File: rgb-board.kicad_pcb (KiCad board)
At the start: 2 copper layers, 178 x 129.5 mm, 89 parts, among them J1 Conn_02x25_Odd_Even, J10 Conn_Coaxial, J11 Conn_Coaxial, J2 SCART-F, J3 TEST_1P, J4 TEST_1P, J5 Conn_Coaxial, J6 Conn_Coaxial, J7 Conn_Coaxial, J8 Conn_Coaxial, J9 Conn_Coaxial, Q101 BC850C, Q105 BC850C, Q109 BC850C, Q113 BC850C, Q114 BC850C, Q201 BC850C, SW1 SW_DPDT_x2, U1 NCP1117-12_SOT223

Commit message: Add files via upload
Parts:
- removed C105: 10uF/50V, Capacitor_SMD:C_Elec_5x5.4
- removed C119: 100nF, Capacitor_SMD:C_0805_2012Metric_Pad1.18x1.45mm_HandSolder
- removed D109, D110: BAT46-TR, Diode_SMD:D_SOD-123
- removed J5, J6, J7, J8, J9: Conn_Coaxial, bnc-tht:BNC-THT
- removed Q114: BC850C, Package_TO_SOT_SMD:SOT-23_Handsoldering
- removed R152: 75, Resistor_SMD:R_0805_2012Metric_Pad1.20x1.40mm_HandSolder
- removed R155: 100, Resistor_SMD:R_0805_2012Metric_Pad1.20x1.40mm_HandSolder
- removed R156, R157: 33k, Resistor_SMD:R_0805_2012Metric_Pad1.20x1.40mm_HandSolder
- removed R158: 2.7k, Resistor_SMD:R_0805_2012Metric_Pad1.20x1.40mm_HandSolder
- added C1: 1uF/16V, Capacitor_SMD:C_Elec_4x5.4, F.Cu at (115.7, 43.4)
- added C2: 1uF/16V, Capacitor_SMD:C_Elec_4x5.4, F.Cu at (115.7, 57.1)
- added C3: 100nF, Capacitor_SMD:C_1206_3216Metric_Pad1.33x1.80mm_HandSolder, F.Cu at (124.8, 56.5)
- added C4: 10nF, Capacitor_SMD:C_1206_3216Metric_Pad1.33x1.80mm_HandSolder, F.Cu at (153.3, 51.6)
- added C5: 10nF, Capacitor_SMD:C_1206_3216Metric_Pad1.33x1.80mm_HandSolder, F.Cu at (137.6, 55.4)
- added C6: 100nF, Capacitor_SMD:C_1206_3216Metric_Pad1.33x1.80mm_HandSolder, F.Cu at (146.5, 56.4)
- added D1: 1N4148W, Diode_SMD:D_SOD-123, F.Cu at (137.6, 47.9)
- added D2: LED_Small_Filled, LED_THT:LED_D5.0mm_Horizontal_O1.27mm_Z3.0mm, F.Cu at (88.5, 66.2)
- added J4: TEST_1P, Mounting_Holes:MountingHole_3.2mm_M3, F.Cu at (97.0, 152.2)
- added J4: TEST_1P, Mounting_Holes:MountingHole_3.2mm_M3, F.Cu at (102.5, 38.2)
- added Q1: BC847B, Package_TO_SOT_SMD:SOT-23_Handsoldering, F.Cu at (132.4, 58.7)
- added R10: 470R, Resistor_SMD:R_1206_3216Metric_Pad1.30x1.75mm_HandSolder, F.Cu at (115.7, 62.2)
- added R11: 1k, Resistor_SMD:R_1206_3216Metric_Pad1.30x1.75mm_HandSolder, F.Cu at (137.6, 51.5)
- added R4: 10k, Resistor_SMD:R_1206_3216Metric_Pad1.30x1.75mm_HandSolder, F.Cu at (115.6, 48.4)
- added R5: 10k, Resistor_SMD:R_1206_3216Metric_Pad1.30x1.75mm_HandSolder, F.Cu at (115.6, 52.1)
- added R6: 2k2, Resistor_SMD:R_1206_3216Metric_Pad1.30x1.75mm_HandSolder, F.Cu at (131.6, 47.0)
- added R7: 1k, Resistor_SMD:R_1206_3216Metric_Pad1.30x1.75mm_HandSolder, F.Cu at (124.7, 60.2)
- added R8: 5k6, Resistor_SMD:R_1206_3216Metric_Pad1.30x1.75mm_HandSolder, F.Cu at (153.3, 45.9)
- added R9: 8k2, Resistor_SMD:R_1206_3216Metric_Pad1.30x1.75mm_HandSolder, F.Cu at (137.7, 44.0)
- added U2: 74HC86, Package_SO:SOIC-14_3.9x8.7mm_P1.27mm, F.Cu at (124.9, 50.5)
- added U3: 74HC123, Package_SO:SOIC-16_3.9x9.9mm_P1.27mm, F.Cu at (146.3, 49.6)
- added X1: VGAF, HD15:HD15_B-HD15F, F.Cu at (92.4, 49.5)
- C114, C116, C117, C118, C121, C201, C202, C204, C205, C206: footprint Capacitor_SMD:C_0805_2012Metric_Pad1.18x1.45mm_HandSolder -> Capacitor_SMD:C_1206_3216Metric_Pad1.33x1.80mm_HandSolder
- C120, C122: footprint Capacitor_SMD:C_Elec_5x5.4 -> Capacitor_SMD:C_Elec_4x5.4
- D101, D102, D103, D104, D105, D106, D107, D108: value BAT46-TR -> BAT46W
- D201: value D_Zener -> BZT52C12
- J10, J11: value Conn_Coaxial -> RCJ-013; footprint rcj-41x:RCJ-04X -> RCJ-013:CUI_RCJ-013
- J3: value TEST_1P -> AudioJack2_Ground_123; footprint Mounting_Holes:MountingHole_3.2mm_M3 -> Connector_PinHeader_2.54mm:PinHeader_1x03_P2.54mm_Vertical
- R1, R105, R106, R107, R119, R120, R121, R133, R134, R135, R147, R148, R149, R2, R204, R3: footprint Resistor_SMD:R_0805_2012Metric_Pad1.20x1.40mm_HandSolder -> Resistor_SMD:R_1206_3216Metric_Pad1.30x1.75mm_HandSolder
- R101, R115, R129, R143: value 75 -> 75R; footprint Resistor_SMD:R_0805_2012Metric_Pad1.20x1.40mm_HandSolder -> Resistor_SMD:R_1206_3216Metric_Pad1.30x1.75mm_HandSolder
- R104, R114, R118, R128, R132, R142, R146: value 100 -> 100R; footprint Resistor_SMD:R_0805_2012Metric_Pad1.20x1.40mm_HandSolder -> Resistor_SMD:R_1206_3216Metric_Pad1.30x1.75mm_HandSolder
- R113, R127, R141: value 390 -> 390R; footprint Resistor_SMD:R_0805_2012Metric_Pad1.20x1.40mm_HandSolder -> Resistor_SMD:R_1206_3216Metric_Pad1.30x1.75mm_HandSolder
- R202: value 1K -> 1k; footprint Resistor_SMD:R_0805_2012Metric_Pad1.20x1.40mm_HandSolder -> Resistor_SMD:R_1206_3216Metric_Pad1.30x1.75mm_HandSolder
- R203: value 56K -> 56k; footprint Resistor_SMD:R_0805_2012Metric_Pad1.20x1.40mm_HandSolder -> Resistor_SMD:R_1206_3216Metric_Pad1.30x1.75mm_HandSolder
- R205: value 2.7K -> 2.7k; footprint Resistor_SMD:R_0805_2012Metric_Pad1.20x1.40mm_HandSolder -> Resistor_SMD:R_1206_3216Metric_Pad1.30x1.75mm_HandSolder
- moved J4 134.4 mm to (98.5, 95.2)
- moved J3 86.1 mm to (98.5, 120.2), turned to 90 degrees
- moved C115 69.8 mm to (154.7, 91.6), turned to 180 degrees
- moved R141 62.5 mm to (145.6, 126.6), turned to 0 degrees
- moved R113 62.5 mm to (145.6, 95.4), turned to 0 degrees
- moved R127 62.4 mm to (145.6, 110.9), turned to 0 degrees
- moved R106 61.7 mm to (134.6, 94.4)
- moved R133 61.7 mm to (140.2, 126.6)
- moved R120 61.7 mm to (134.6, 109.9)
- moved R134 61.7 mm to (134.6, 125.6)
- moved R119 61.7 mm to (140.1, 110.9)
- moved R105 61.7 mm to (140.1, 95.4)
- moved R142 61.5 mm to (145.6, 122.6)
- moved R128 61.4 mm to (145.6, 106.9)
- moved R114 61.3 mm to (145.6, 91.4)
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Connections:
- net /B/B-Y renamed /B/B-Y
- net /G/Y renamed /G/Y
- net /HD/CS renamed /HD/CS
- net /R/R-Y renamed /R/R-Y
- J1 pad 10: (no net) -> unconnected-(J1-Pad10)
- J1 pad 15: (no net) -> unconnected-(J1-Pad15)
- J1 pad 16: (no net) -> unconnected-(J1-Pad16)
- J1 pad 17: (no net) -> unconnected-(J1-Pad17)
- J1 pad 18: (no net) -> unconnected-(J1-Pad18)
- J1 pad 20: (no net) -> unconnected-(J1-Pad20)
- J1 pad 22: (no net) -> unconnected-(J1-Pad22)
- J1 pad 23: (no net) -> unconnected-(J1-Pad23)
- J1 pad 24: (no net) -> unconnected-(J1-Pad24)
- J1 pad 26: (no net) -> unconnected-(J1-Pad26)
- J1 pad 27: (no net) -> unconnected-(J1-Pad27)
- J1 pad 28: (no net) -> unconnected-(J1-Pad28)
- J1 pad 29: (no net) -> unconnected-(J1-Pad29)
- J1 pad 30: (no net) -> unconnected-(J1-Pad30)
- J1 pad 32: (no net) -> unconnected-(J1-Pad32)
- J1 pad 33: (no net) -> unconnected-(J1-Pad33)
- J1 pad 34: (no net) -> unconnected-(J1-Pad34)
- J1 pad 35: (no net) -> unconnected-(J1-Pad35)
- J1 pad 36: (no net) -> unconnected-(J1-Pad36)
- J1 pad 37: (no net) -> unconnected-(J1-Pad37)
- J1 pad 38: (no net) -> unconnected-(J1-Pad38)
- J1 pad 40: (no net) -> unconnected-(J1-Pad40)
- J1 pad 42: (no net) -> unconnected-(J1-Pad42)
- J1 pad 43: (no net) -> unconnected-(J1-Pad43)
- J1 pad 44: (no net) -> unconnected-(J1-Pad44)
- J1 pad 45: (no net) -> unconnected-(J1-Pad45)
- J1 pad 46: (no net) -> unconnected-(J1-Pad46)
- J1 pad 8: (no net) -> unconnected-(J1-Pad8)
- J1 pad 9: (no net) -> unconnected-(J1-Pad9)
- J10 pad 2: GND -> /AUDIO_EXT_R
- J11 pad 2: GND -> /AUDIO_EXT_L
- J2 pad 1: (no net) -> unconnected-(J2-Pad1)
- J2 pad 10: (no net) -> unconnected-(J2-Pad10)
- J2 pad 12: (no net) -> unconnected-(J2-Pad12)
- J2 pad 14: (no net) -> unconnected-(J2-Pad14)
- J2 pad 16: (no net) -> unconnected-(J2-Pad16)
- J2 pad 19: (no net) -> unconnected-(J2-Pad19)
- J2 pad 3: (no net) -> unconnected-(J2-Pad3)
- J2 pad 8: (no net) -> unconnected-(J2-Pad8)
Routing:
- net /VD_: track 141.6 -> 0.00 mm
- net +5V: track 0.00 -> 123.6 mm, vias 0 -> 3
- net Net-(R4-Pad2): track 0.00 -> 105.8 mm, vias 0 -> 3
- net Net-(D1-Pad1): track 0.00 -> 80.2 mm, vias 0 -> 2
- net /B/B-Y: track 28.7 -> 96.0 mm, vias 0 -> 1
- net Net-(R5-Pad2): track 0.00 -> 55.5 mm, vias 0 -> 1
- net /R/R-Y: track 46.4 -> 97.8 mm
- net /G/Y: track 40.4 -> 76.9 mm, vias 0 -> 1
- net /Y: track 120.9 -> 91.2 mm, vias 0 -> 1
- net Net-(D2-Pad1): track 0.00 -> 29.1 mm
- net Net-(U2-Pad3): track 0.00 -> 26.1 mm, vias 0 -> 2
- net /AUDIO_: track 113.6 -> 90.7 mm, vias 0 -> 1
- net Net-(Q1-Pad3): track 0.00 -> 22.2 mm, vias 0 -> 2
- net /VCC+14V: track 81.8 -> 59.6 mm, vias 0 -> 1
- net Net-(C5-Pad1): track 0.00 -> 21.5 mm, vias 0 -> 2
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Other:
- board size 178 x 129.5 mm -> 145 x 130 mm
- net class Default removed
- rule pad_to_mask_clearance: 0.2 -> 0
- board text added: "1080/1035"
- board text added: "AUDIO"
- board text added: "All resistors and MLCC caps are 1206 R1,2,10: 470 Ω R3: 20 kΩ R4,5: 10 kΩ R6: 2.2 kΩ R7,11,202: 1 kΩ R8: 5.6 kΩ R9: 8.2 kΩ R101,115,129,143: 75 Ω R104,114,118,128,132,142,146: 100 Ω R105,119,133,203: 56 kΩ R106,120,134,147,148: 33 kΩ R107,121,135: 1.5 kΩ R113,127,141: 390 Ω R149,205: 2.7 kΩ R204: 68 kΩ"
- board text added: "BGP(HD)"
- board text added: "Blue"
- board text added: "C1,2: 1µF/16V E-cap C3,6,114,116,117,118,206: 100 nF/25V MLCC C4,5: 10nF MLCC C101,102,103: 47µF/25V E-cap C104: 10µF/50V E-cap C115,207: 100 µF/16V E-Cap C120,122: 10µF/25V E-cap C121: 1 µF/25V MLCC C201,202,205: 180 pF MLCC C203: 1 µF/50V E-Cap C204: 39 pF MLCC"
- board text added: "C_IN(VIDEO)"
- board text added: "D101-D108: BAT46W (SOD-123) D201: BZT52C12 (12V Zener, SOD-123) D1: 1N4148W (SOD-123) D2: 5 mm LED Q1,101,105,109,113,201: BC847B (SOT-23)"
- board text added: "FSC CL/BW"
- board text added: "Green"
- board text added: "H-Sync"
- board text added: "HD VD"
- board text added: "H_BLK"
- board text added: "INPUT_A/B"
- board text added: "In Audio L In Audio R GND"
- board text added: "JVC IF-C01COMG (RGB/YPbPr) SCART/VGA 15kHz SMD CLONE BOARD (2021) Martin Hejnfelt (martin@hejnfelt.com) (2024) makotoworkshop.org"
- board text added: "NTSC/PAL"
- board text added: "ON - EXTERNAL STEREO OFF - INTERNAL MONO"
- board text added: "Red"
- board text added: "SDA SCL"
- board text added: "SLOT_SCA1 SLOT_SCA2 SLOT_SCA3 SLOT_SCA4 SLOT_DET"
- board text added: "To protect the CRT If VGA signal is not 15kHz HD/CS and LED are OFF"
- board text added: "V-Sync"
- board text added: "VCC+14V VCC+14V"
- board text added: "VCC+7V VCC+7V"
- board text added: "Vin Sync"
- board text added: "X1: VGAF (SUB-D 15 HD) J1: Pin Header Angled 2x25 J2: SCART Ninigi right angled J3: Pin Header 1x3 J10,11: RCA AV RCJ-013 CUDevices SW1: LC2259EENP U1: NCP1117-12 (SOT-223) U2: 74HC86 (SOP-14) U3: 74HC123 (SOP-16)"
- board text added: "Y B-Y R-Y"
- board text added: "YC_DET"
- board text added: "in Audio L"
- board text added: "in Audio R"
- board text removed: "Bridge here for input (BNC) and don't mount SW1"
- board text removed: "D101-D110: BAT46W (SOD-123) D201: BZT52C12 (12V Zener, SOD-123) All transistors (Q101, Q102, ...): BC850 C101,102,103: 47uF/25V E-cap C104,105,120,122: 10uF/25V E-cap C115,207: 100 uF/16V E-Cap C114,116,117,118,119,206: 100 nF/25V MLCC C203: 1 uF/50V E-Cap C121: 1 uF/25V MLCC C201,202,205: 180 pF MLCC C204: 39 pF MLCC MLCC caps are 0805 R101,115,129,143,152: 75 Ohm R104,114,118,128,132,142,146,15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"
- board text removed: "Do NOT mount this section when using SCART"
- board text removed: "JVC IF-C01COMG (RGB/YPbPr) SCART/BNC SMD CLONE BOARD (2021) Martin Hejnfelt (martin@hejnfelt.com) Dual input idea credit goes to James Vanderloeff!"
- board text removed: "SW1 IN - EXTERNAL STEREO OUT - INTERNAL MONO"
- board text removed: "VD"

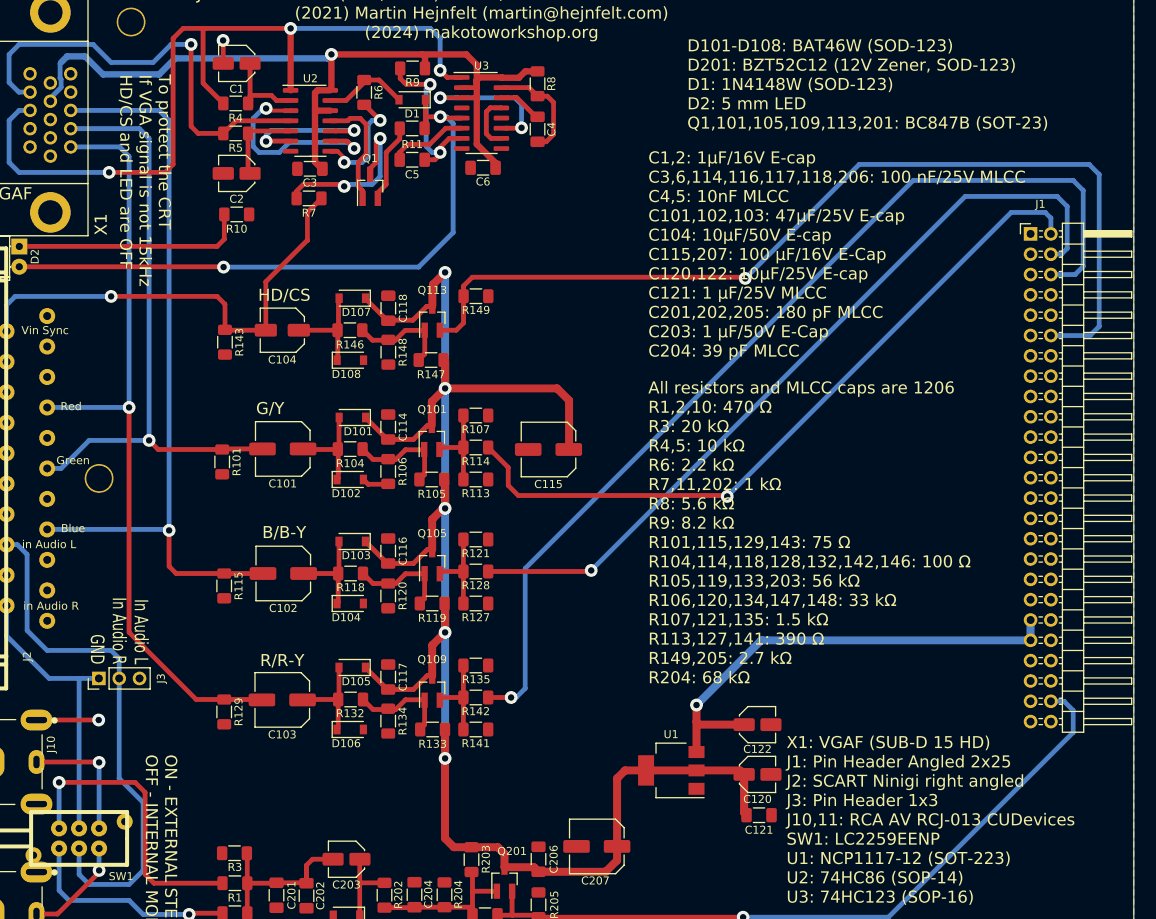
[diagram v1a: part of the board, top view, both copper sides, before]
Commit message: Update rgb-board.kicad_pcb
5V-corrigé
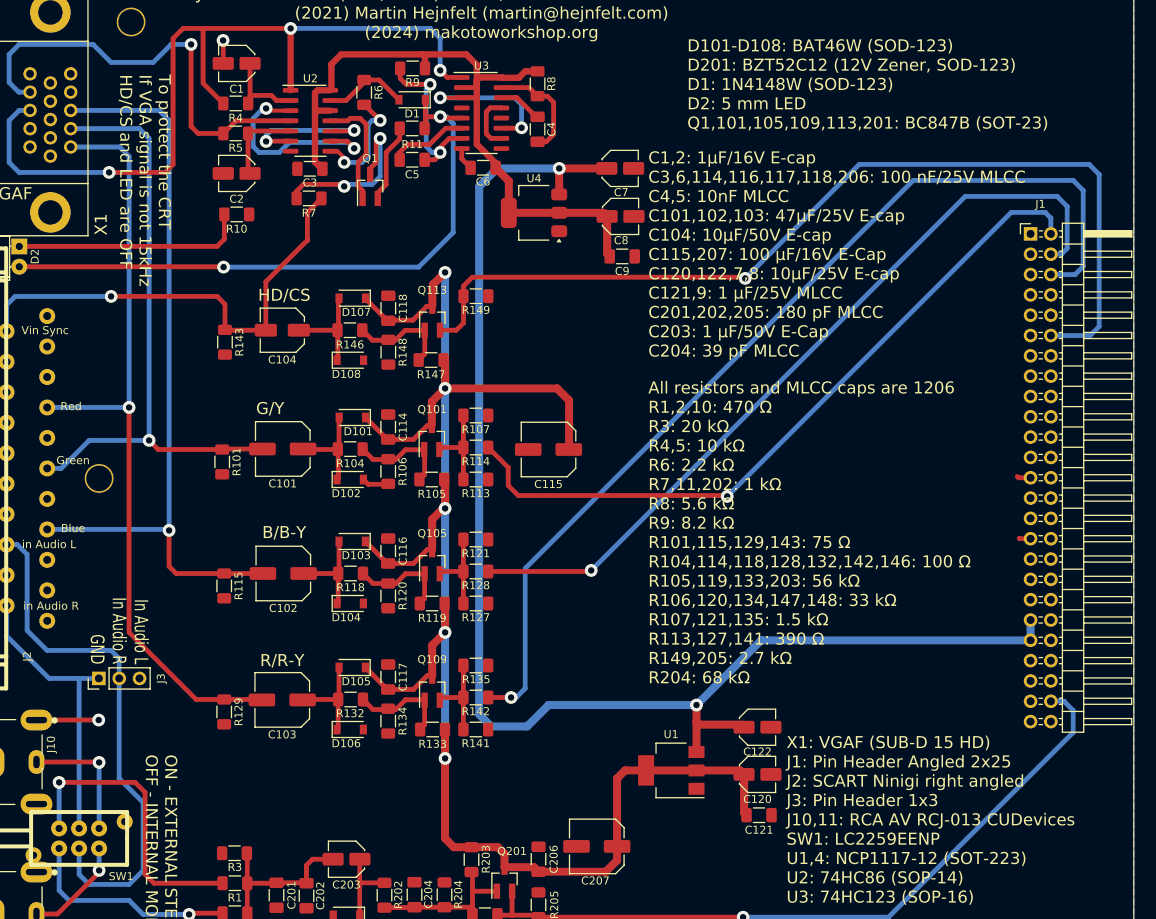
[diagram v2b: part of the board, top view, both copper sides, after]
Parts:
- added C7: 10uF/25V, Capacitor_SMD:C_Elec_4x5.4, F.Cu at (163.6, 56.5)
- added C8: 10uF/25V, Capacitor_SMD:C_Elec_4x5.4, F.Cu at (163.7, 62.5)
- added C9: 1uF/25V, Capacitor_SMD:C_1206_3216Metric_Pad1.33x1.80mm_HandSolder, F.Cu at (163.9, 67.5)
- added U4: NCP1117-5_SOT223, Package_TO_SOT_SMD:SOT-223-3_TabPin2, F.Cu at (152.8, 62.0)
- moved C122 0.33 mm to (180.8, 126.4)
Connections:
- X1 pad 9: +5V -> unconnected-(X1-Pad9)
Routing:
- net /VCC+14V: track 59.6 -> 174.7 mm, vias 1 -> 2
- net +5V: track 123.6 -> 105.9 mm, vias 3 -> 2
- net GND: track 14.1 -> 20.1 mm
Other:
- board text added: "C1,2: 1µF/16V E-cap C3,6,114,116,117,118,206: 100 nF/25V MLCC C4,5: 10nF MLCC C101,102,103: 47µF/25V E-cap C104: 10µF/50V E-cap C115,207: 100 µF/16V E-Cap C120,122,7,8: 10µF/25V E-cap C121,9: 1 µF/25V MLCC C201,202,205: 180 pF MLCC C203: 1 µF/50V E-Cap C204: 39 pF MLCC"
- board text added: "X1: VGAF (SUB-D 15 HD) J1: Pin Header Angled 2x25 J2: SCART Ninigi right angled J3: Pin Header 1x3 J10,11: RCA AV RCJ-013 CUDevices SW1: LC2259EENP U1,4: NCP1117-12 (SOT-223) U2: 74HC86 (SOP-14) U3: 74HC123 (SOP-16)"
- board text removed: "C1,2: 1µF/16V E-cap C3,6,114,116,117,118,206: 100 nF/25V MLCC C4,5: 10nF MLCC C101,102,103: 47µF/25V E-cap C104: 10µF/50V E-cap C115,207: 100 µF/16V E-Cap C120,122: 10µF/25V E-cap C121: 1 µF/25V MLCC C201,202,205: 180 pF MLCC C203: 1 µF/50V E-Cap C204: 39 pF MLCC"
- board text removed: "X1: VGAF (SUB-D 15 HD) J1: Pin Header Angled 2x25 J2: SCART Ninigi right angled J3: Pin Header 1x3 J10,11: RCA AV RCJ-013 CUDevices SW1: LC2259EENP U1: NCP1117-12 (SOT-223) U2: 74HC86 (SOP-14) U3: 74HC123 (SOP-16)"
